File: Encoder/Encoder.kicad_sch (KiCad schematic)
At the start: 10 parts, among them J1 Conn_01x04_Socket, J2 Conn_01x04_Socket

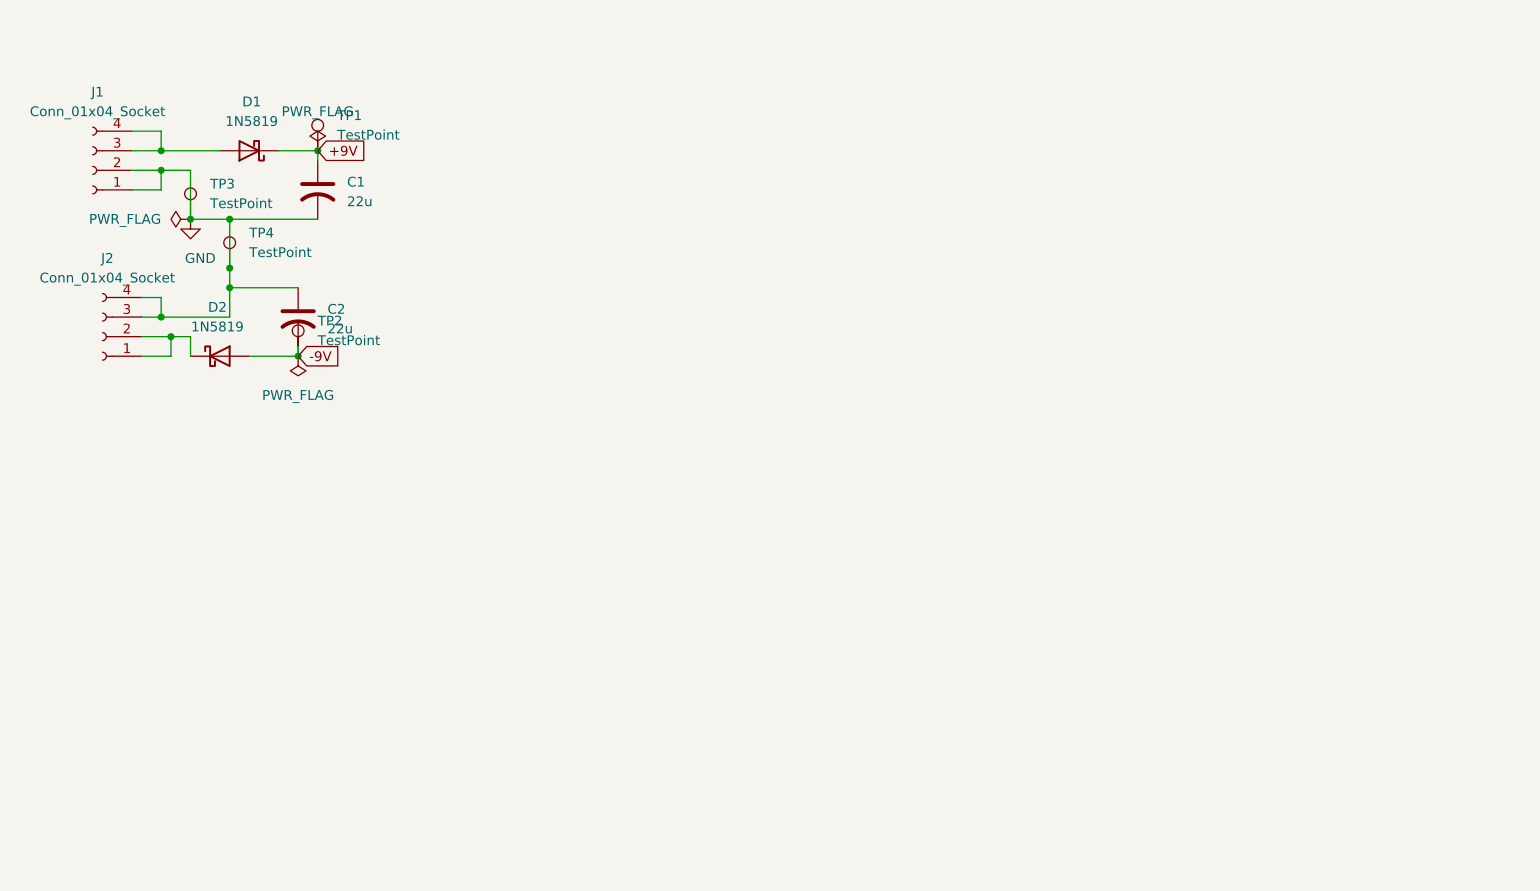
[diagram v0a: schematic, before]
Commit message: added the filter for L and R
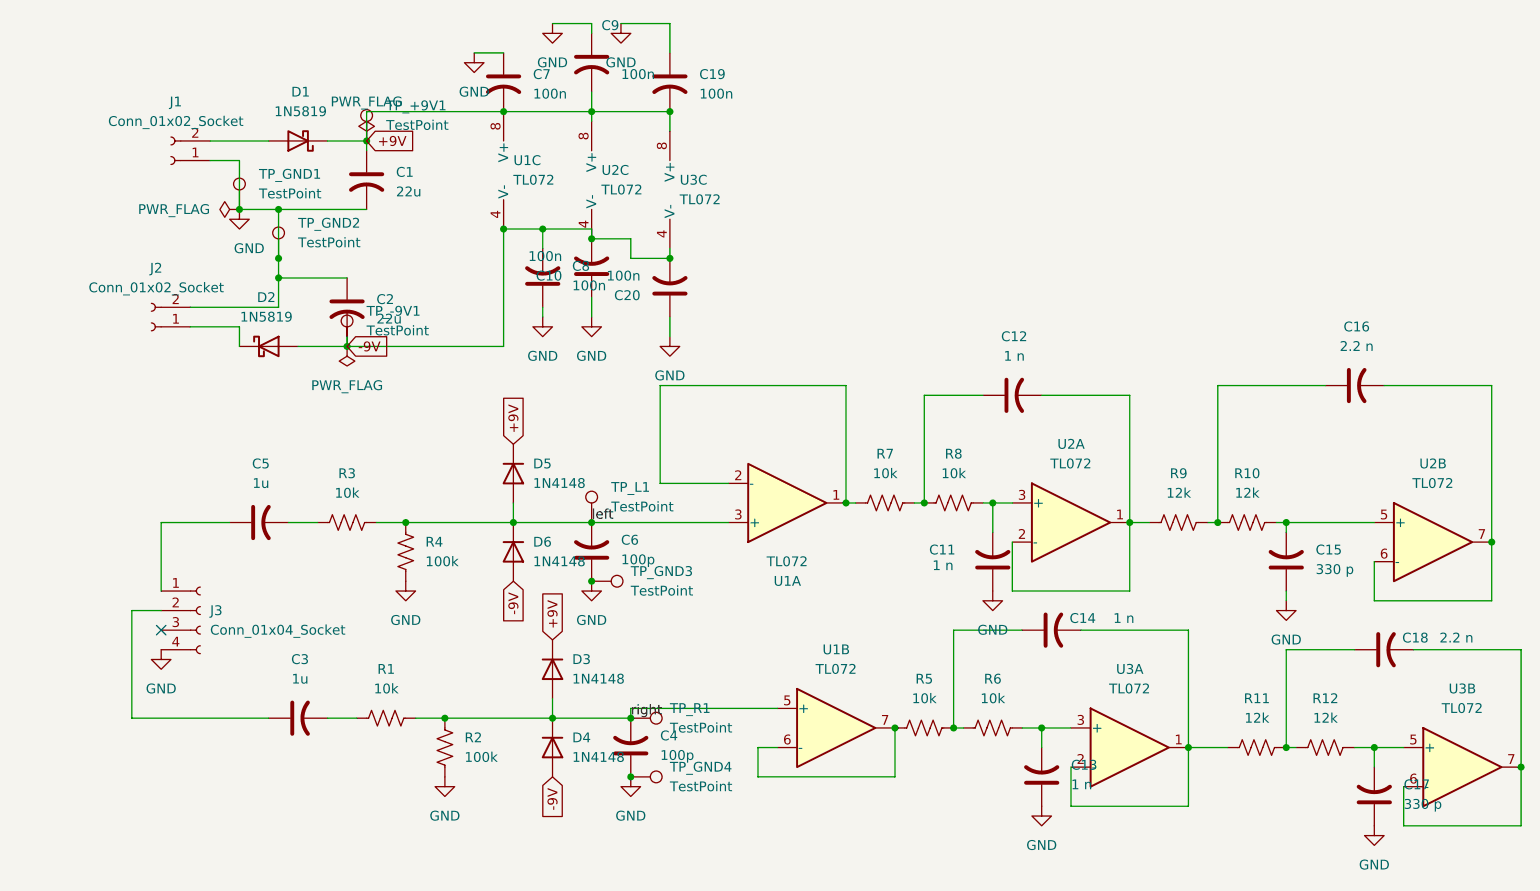
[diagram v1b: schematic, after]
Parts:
- removed J1, J2: Conn_01x04_Socket, Connector_PinSocket_2.54mm:PinSocket_1x04_P2.54mm_Vertical, symbol Connector:Conn_01x04_Socket
- added C10, C19, C20, C7, C8, C9: 100n, Capacitor_THT:C_Disc_D5.0mm_W2.5mm_P5.00mm, symbol Device:C_US
- added C11, C12, C13, C14: 1 n, Capacitor_THT:C_Disc_D5.0mm_W2.5mm_P5.00mm, symbol Device:C_US
- added C15, C17: 330 p, Capacitor_THT:C_Disc_D5.0mm_W2.5mm_P5.00mm, symbol Device:C_US
- added C16, C18: 2.2 n, Capacitor_THT:C_Disc_D5.0mm_W2.5mm_P5.00mm, symbol Device:C_US
- added C3, C5: 1u, Capacitor_THT:C_Rect_L7.2mm_W3.5mm_P5.00mm, symbol Device:C_US
- added C4, C6: 100p, Capacitor_THT:C_Disc_D3.0mm_W2.0mm_P2.50mm, symbol Device:C_US
- added D3, D4, D5, D6: 1N4148, Diode_THT:D_DO-35_SOD27_P7.62mm_Horizontal, symbol Diode:1N4148
- added J1, J2: Conn_01x02_Socket, TerminalBlock_Phoenix:TerminalBlock_Phoenix_MKDS-1,5-2-5.08_1x02_P5.08mm_Horizontal, symbol Connector:Conn_01x02_Socket
- added J3: Conn_01x04_Socket, Connector_PinSocket_2.54mm:PinSocket_1x04_P2.54mm_Vertical, symbol Connector:Conn_01x04_Socket
- added R1, R3, R5, R6, R7, R8: 10k, Resistor_THT:R_Axial_DIN0207_L6.3mm_D2.5mm_P10.16mm_Horizontal, symbol Device:R_US
- added R10, R11, R12, R9: 12k, Resistor_THT:R_Axial_DIN0207_L6.3mm_D2.5mm_P10.16mm_Horizontal, symbol Device:R_US
- added R2, R4: 100k, Resistor_THT:R_Axial_DIN0207_L6.3mm_D2.5mm_P10.16mm_Horizontal, symbol Device:R_US
- added TP_GND3, TP_GND4, TP_L1, TP_R1: TestPoint, TestPoint:TestPoint_Pad_D1.5mm, symbol Connector:TestPoint
- added U1, U2, U3: TL072, Package_DIP:DIP-8_W7.62mm_Socket, symbol Amplifier_Operational:TL072
- renumbered TP1 to TP_+9V1, TP2 to TP_-9V1, TP3 to TP_GND1, TP4 to TP_GND2
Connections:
- net +9V: now also C19.2, C7.2, C9.2, D3.1 (K), D5.1 (K), U1.8 (V+), U2.8 (V+), U3.8 (V+)
- net -9V: now also C10.2, C20.2, C8.2, D4.2 (A), D6.2 (A), U1.4 (V-), U2.4 (V-), U3.4 (V-)
- net GND: now also C10.1, C11.1, C13.1, C15.1, C17.1, C19.1, C20.1, C4.1, C6.1, C7.1, C8.1, C9.1, J1.1 (Pin_1), J2.2 (Pin_2), J3.4 (Pin_4), R2.2, R4.2, TP_GND3.1, TP_GND4.1
- net at D2.1 (K): now also J2.1 (Pin_1)
- net at D1.2 (A): now also J1.2 (Pin_2)
- new net: C14.1, R5.2, R6.1
- new net: C14.2, R11.1, U3.1, U3.2 (-)
- new net: C3.2, R1.1
- new net: R5.1, U1.6 (-), U1.7
- new net: C12.1, R7.2, R8.1
- new net: C11.2, R8.2, U2.3 (+)
- new net: C18.1, R11.2, R12.1
- new net: C17.2, R12.2, U3.5 (+)
- new net: C5.1, J3.1 (Pin_1)
- new net: C3.1, J3.2 (Pin_2)
- new net: C18.2, U3.6 (-), U3.7
- new net: C5.2, R3.1
- new net: C12.2, R9.1, U2.1, U2.2 (-)
- new net: C15.2, R10.2, U2.5 (+)
- new net: C16.2, U2.6 (-), U2.7
- new net: C13.2, R6.2, U3.3 (+)
- new net: C16.1, R10.1, R9.2
- new net: R7.1, U1.1, U1.2 (-)
- new net left: C6.2, D5.2 (A), D6.1 (K), R3.2, R4.1, TP_L1.1, U1.3 (+)
- new net right: C4.2, D3.2 (A), D4.1 (K), R1.2, R2.1, TP_R1.1, U1.5 (+)
- no-connect marks 0 -> 1
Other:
- moved on the sheet: C1, C2, D1, D2, TP_+9V1, TP_-9V1, TP_GND1, TP_GND2

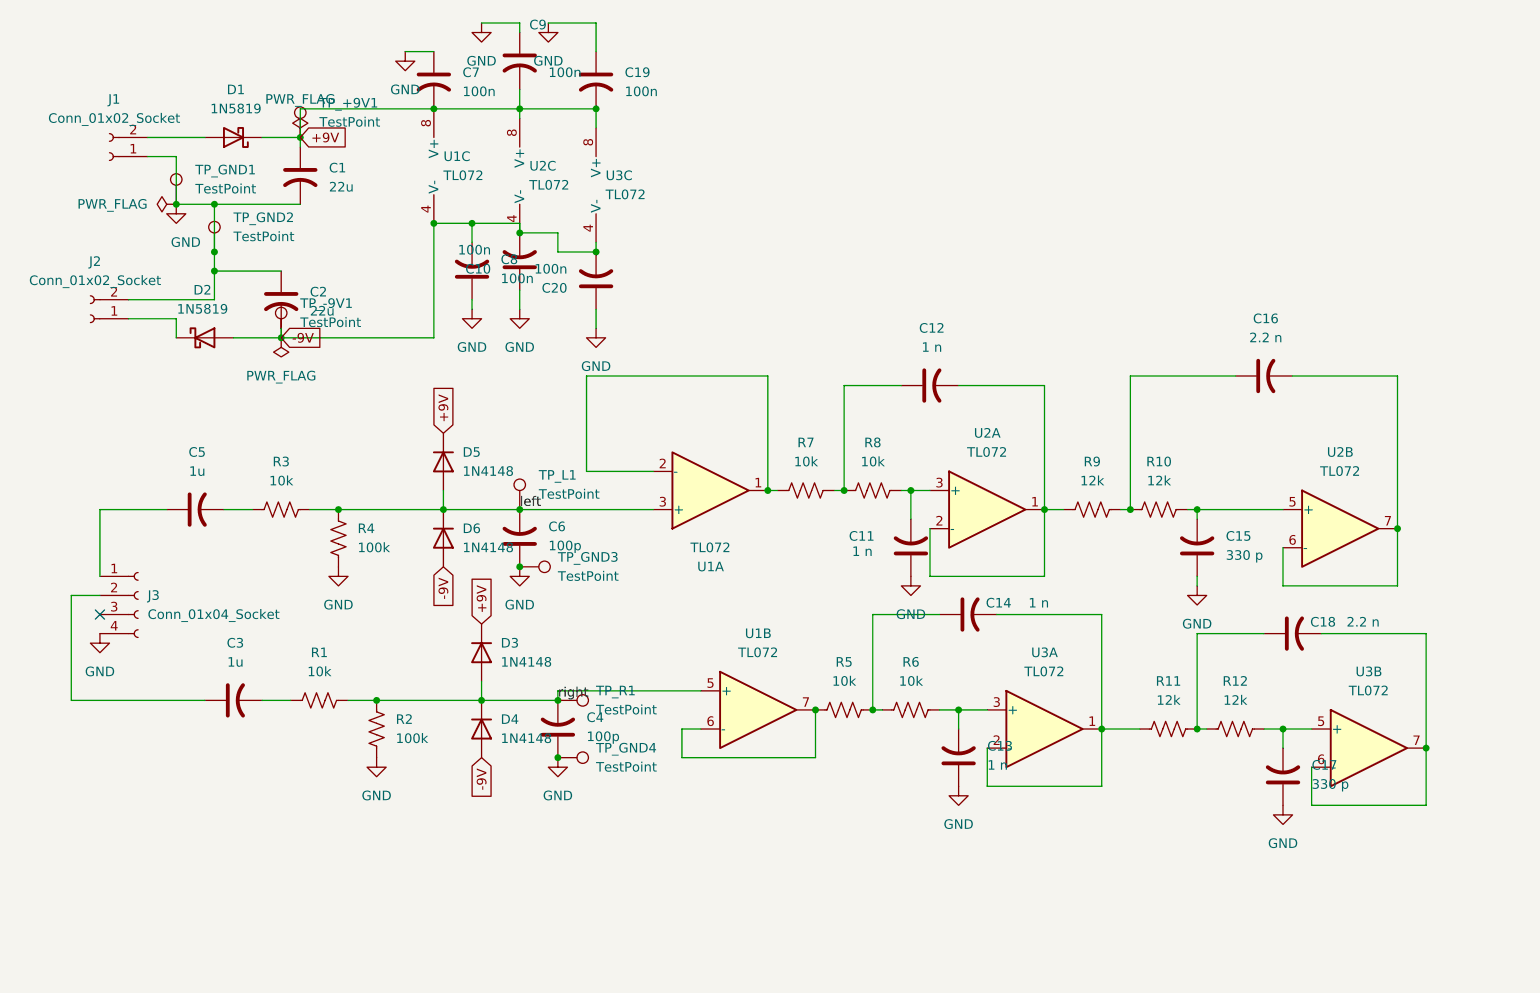
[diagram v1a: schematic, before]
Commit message: added the filter for L and R
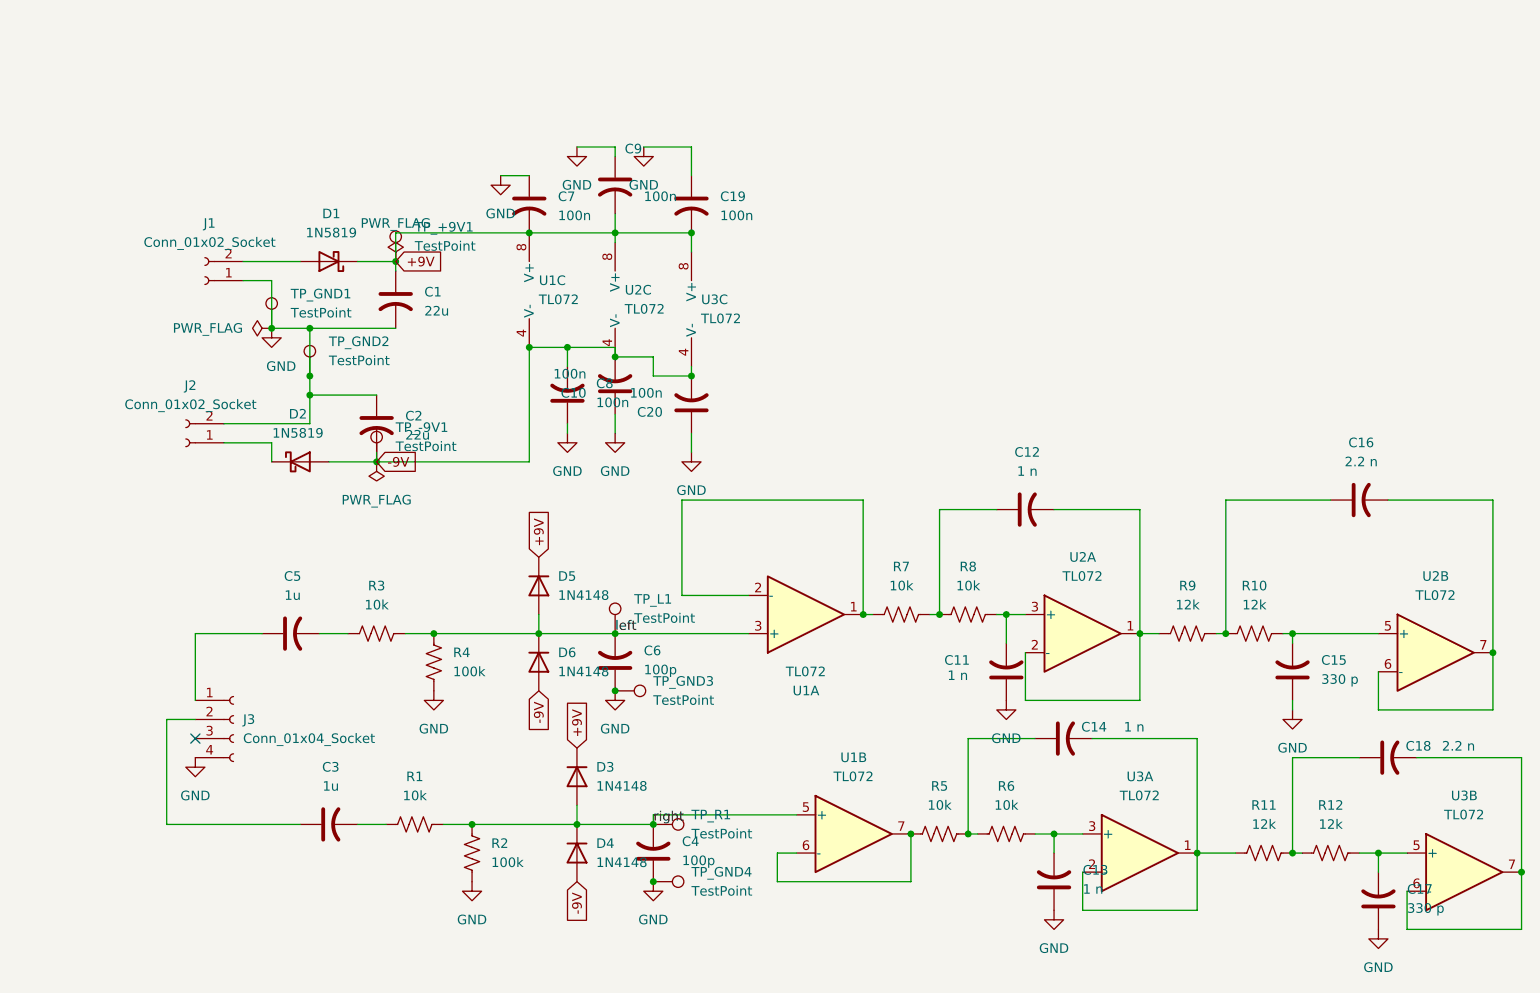
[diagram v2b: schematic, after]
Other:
- moved on the sheet: C1, C10, C11, C12, C13, C14, C15, C16, C17, C18, C19, C2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

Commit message: schematics almost done
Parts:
- added C21, C22, C23, C24, C25, C26, C27, C28, C29, C30, C31, C38, C39, C40, C41: 100n, Capacitor_THT:C_Disc_D5.0mm_W2.5mm_P5.00mm, symbol Device:C_US
- added C32, C35: 1n, Capacitor_THT:C_Disc_D5.0mm_W2.5mm_P5.00mm, symbol Device:C_US
- added C33: 1.2n, Capacitor_THT:C_Disc_D5.0mm_W2.5mm_P5.00mm, symbol Device:C_US
- added C34: 2.2n, Capacitor_THT:C_Disc_D5.0mm_W2.5mm_P5.00mm, symbol Device:C_US
- added C36: 3.3n, Capacitor_THT:C_Disc_D5.0mm_W2.5mm_P5.00mm, symbol Device:C_US
- added C37: 220P, Capacitor_THT:C_Disc_D5.0mm_W2.5mm_P5.00mm, symbol Device:C_US
- added R13, R14, R15, R16, R17, R18, R34, R35, R36, R37, R38: 100k, Resistor_THT:R_Axial_DIN0207_L6.3mm_D2.5mm_P10.16mm_Horizontal, symbol Device:R_US
- added R19, R21: 51, Resistor_THT:R_Axial_DIN0207_L6.3mm_D2.5mm_P10.16mm_Horizontal, symbol Device:R_US
- added R20, R29, R31: 1k, Resistor_THT:R_Axial_DIN0207_L6.3mm_D2.5mm_P10.16mm_Horizontal, symbol Device:R_US
- added R22: 6.8k, Resistor_THT:R_Axial_DIN0207_L6.3mm_D2.5mm_P10.16mm_Horizontal, symbol Device:R_US
- added R23, R24: 3.9k, Resistor_THT:R_Axial_DIN0207_L6.3mm_D2.5mm_P10.16mm_Horizontal, symbol Device:R_US
- added R25, R26, R27, R28: 15k, Resistor_THT:R_Axial_DIN0207_L6.3mm_D2.5mm_P10.16mm_Horizontal, symbol Device:R_US
- added R30: 10k, Resistor_THT:R_Axial_DIN0207_L6.3mm_D2.5mm_P10.16mm_Horizontal, symbol Device:R_US
- added R32: 7.5k, Resistor_THT:R_Axial_DIN0207_L6.3mm_D2.5mm_P10.16mm_Horizontal, symbol Device:R_US
- added R33: 2.2k, Resistor_THT:R_Axial_DIN0207_L6.3mm_D2.5mm_P10.16mm_Horizontal, symbol Device:R_US
- added R39, R40: 2.4k, Resistor_THT:R_Axial_DIN0207_L6.3mm_D2.5mm_P10.16mm_Horizontal, symbol Device:R_US
- added R41, R42: 1.8k, Resistor_THT:R_Axial_DIN0207_L6.3mm_D2.5mm_P10.16mm_Horizontal, symbol Device:R_US
- added R43, R44: 3.3k, Resistor_THT:R_Axial_DIN0207_L6.3mm_D2.5mm_P10.16mm_Horizontal, symbol Device:R_US
- added R45, R48, R49, R50: 100K, Resistor_THT:R_Axial_DIN0207_L6.3mm_D2.5mm_P10.16mm_Horizontal, symbol Device:R_US
- added R46: 270K, Resistor_THT:R_Axial_DIN0207_L6.3mm_D2.5mm_P10.16mm_Horizontal, symbol Device:R_US
- added R47: 360K, Resistor_THT:R_Axial_DIN0207_L6.3mm_D2.5mm_P10.16mm_Horizontal, symbol Device:R_US
- added unit 2 of U2
- added unit 2 of U3
- added U4, U7, U9: TL072, Package_DIP:DIP-8_W7.62mm_Socket, symbol Amplifier_Operational:TL072
- added U5: MC1496, Package_DIP:DIP-14_W7.62mm_Socket, symbol MC1496_custom:MC1496
- added U6, U8: NE5532, Package_DIP:DIP-8_W7.62mm_Socket, symbol Amplifier_Operational:NE5532
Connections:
- net +9V: now also C21.2, C26.2, C30.2, C38.2, C39.2, R23.1, R24.1, R32.1, U4.8 (V+), U6.8 (V+), U7.8 (V+), U8.8 (V+), U9.8 (V+)
- net -9V: now also C22.2, C25.1, C31.1, C40.1, C41.1, U4.4 (V-), U5.14 (VEE), U6.4 (V-), U7.4 (V-), U8.4 (V-), U9.4 (V-)
- net GND: now also C21.1, C22.1, C25.2, C26.1, C28.1, C29.1, C30.1, C31.2, C32.2, C35.1, C37.2, C38.1, C39.1, C40.2, C41.2, R15.2, R21.2, R22.2, R27.1, R33.2, U4.5 (+), U7.3 (+), U7.5 (+), U9.3 (+), U9.5 (+)
- net at C17.2, R12.2: now also U3.5 (+); no longer U3.5 (+)
- net at C15.2, R10.2: now also U2.5 (+); no longer U2.5 (+)
- new net: C34.2, R43.1, U8.1, U8.3 (+)
- new net: C35.2, R42.2, U8.2 (-)
- new net: R36.2, R37.1, U7.1
- new net: R37.2, R38.1, U7.6 (-)
- new net: C34.1, R41.2, R42.1
- new net: C27.1, R29.1, U5.8 (VC+)
- new net: R29.2, R31.1
- new net: C33.1, R39.1, R40.2
- new net: C33.2, R41.1, U6.6 (-), U6.7
- new net: R17.2, R18.1, U4.6 (-)
- new net: R18.2, R19.1, U4.7
- new net: R38.2, R45.1, U7.7
- new net: R45.2, R46.2, R47.2, R48.1, U9.2 (-)
- new net: R48.2, R49.1, U9.1
- new net: R26.1, R28.1, U6.2 (-)
- new net: C24.2, R26.2
- new net: R49.2, R50.1, U9.6 (-)
- new net: R40.1, R50.2, U9.7
- new net: R16.2, R17.1, U4.1
- new net: R22.1, U5.5 (Bias)
- new net: R19.2, U5.1 (VS+)
- new net: C18.2, R14.1, R35.1, U3.6 (-), U3.7
- new net: C16.2, R13.1, R34.1, U2.6 (-), U2.7
- new net: R13.2, R16.1, U4.2 (-)
- new net: C32.1, R39.2, U6.5 (+)
- new net: C28.2, C29.2, R31.2, R32.2, R33.1, U5.10 (VC-)
- new net: R28.2, R46.1, U6.1
- new net: C36.1, R43.2, R44.1
- new net: R25.2, R27.2, U6.3 (+)
- new net: R14.2, R15.1, U4.3 (+)
- new net: R34.2, R35.2, R36.1, U7.2 (-)
- new net: C36.2, U8.5 (+), U8.7
- new net: C37.1, R44.2, U8.6 (-)
- new net: R20.1, U5.2 (GAIN2)
- new net: R20.2, U5.3 (GAIN3)
- new net: C27.2, R30.1
- new net: C23.1, R24.2, U5.12 (VO-)
- new net: R21.1, U5.4 (VS-)
- new net: C24.1, R23.2, U5.6 (VO+)
- new net: C23.2, R25.1
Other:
- moved on the sheet: C1, C10, C11, C12, C13, C14, C15, C16, C17, C18, C19, C2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
